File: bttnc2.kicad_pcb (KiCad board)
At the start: 2 copper layers, 72 parts, among them K1 MK12C02, P1 ISP, P2 BATTERY, P3 BNC, P4 USB_OTG, SW1 SW_PUSH, U1 HC-05, U2 APE8800N, U3 BU33TD3WG, U4 ATMEGA328P-AU, U5 DRA818V, U6 DW01-P, U7 TP4056, U8 8205A, X1 QKT-3225SMD 16.0000MHz

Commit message: Update bttnc project. Sch and Pcb files.
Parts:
- added C25: C, Capacitors_SMD:C_0805, B.Cu at (140.9, 109.5)
- added C26: C, Capacitors_SMD:C_0805, B.Cu at (135.3, 116.5)
- added C27: CP1, Capacitors_SMD:C_1206, F.Cu at (158.4, 130.7)
- added C28: C, Capacitors_SMD:C_0805, B.Cu at (158.4, 132.0)
- added C29: C, Capacitors_SMD:C_0805, F.Cu at (159.5, 136.9)
- added C30: CP1, Capacitors_SMD:C_1206, F.Cu at (159.5, 134.5)
- added C31: C, Capacitors_SMD:C_0805, B.Cu at (149.9, 128.5)
- added C32: CP1, Capacitors_SMD:C_1206, B.Cu at (152.3, 129.0)
- added D10: D_Schottky, Diodes_SMD:MiniMELF_Standard, B.Cu at (158.0, 127.3)
- added D11: D_Schottky, Diodes_SMD:MiniMELF_Standard, B.Cu at (155.3, 127.3)
- added D5: D_Schottky, Diodes_SMD:MiniMELF_Standard, B.Cu at (159.9, 107.7)
- added D6: D_Schottky, Diodes_SMD:MiniMELF_Standard, B.Cu at (124.7, 120.6)
- added D7: D_Schottky, Diodes_SMD:MiniMELF_Standard, B.Cu at (155.3, 133.0)
- added D8: LED, LEDs:LED_0805, F.Cu at (104.5, 137.9)
- added D9: D_Schottky, Diodes_SMD:MiniMELF_Standard, B.Cu at (149.7, 133.0)
- added Q1: MMBT3904, TO_SOT_Packages_SMD:SOT-23, B.Cu at (107.8, 137.8)
- added R19: R, Resistors_SMD:R_0805, B.Cu at (125.5, 122.9)
- added R20: R, Resistors_SMD:R_0805, B.Cu at (138.9, 121.7)
- added R21: R, Resistors_SMD:R_0805, F.Cu at (138.4, 116.5)
- added R22: R, Resistors_SMD:R_0805, B.Cu at (151.6, 124.6)
- added R23: R, Resistors_SMD:R_0805, B.Cu at (108.2, 134.9)
- added R24: R, Resistors_SMD:R_0805, B.Cu at (148.0, 128.4)
- added R25: R, Resistors_SMD:R_0805, B.Cu at (160.9, 129.8)
- added R26: R, Resistors_SMD:R_0805, F.Cu at (159.4, 124.6)
- added R27: R, Resistors_SMD:R_0805, B.Cu at (160.9, 126.4)
- added U10: Quectel-L80, footprints:Qectel-L80, F.Cu at (147.6, 130.9)
- added U11: FDG6342L, TO_SOT_Packages_SMD:SC-70-6, F.Cu at (159.4, 127.0)
- added U9: LM358, SMD_Packages:SOIC-8-N, B.Cu at (139.0, 116.3)
- C1, C15, C16, C17, C19, C2, C22, C23, C24, C3, C5, C6, C7, C8, C9, FB1, FB2, FB3, FB6, FB8, R12, R13, R15, R17, R18, R3, R4, R5, R8, R9, U2, U3, U4, U7, U8, X1: moved to B.Cu
- P3: footprint SMD_Packages:SOIC-8-N -> footprints:CON-SMA-EDGE
- SW1: footprint footprints:B3FS-1002P -> Buttons_Switches_ThroughHole:SW_Tactile_SPST_Angled
- moved K1 217.4 mm to (166.4, 139.9)
- moved U8 214.9 mm to (166.5, 135.9), turned to 180 degrees
- moved P2 213.2 mm to (169.4, 129.5), turned to 270 degrees
- moved C20 212.7 mm to (164.8, 134.4)
- moved C19 212.2 mm to (167.2, 130.6), turned to 270 degrees
- moved U6 210.8 mm to (164.9, 131.3), turned to 270 degrees
- moved R12 210.3 mm to (165.0, 130.4), turned to 90 degrees
- moved R14 208.8 mm to (162.3, 131.3), turned to 270 degrees
- moved P4 208.1 mm to (168.6, 122.0), turned to 90 degrees
- moved R18 207.5 mm to (163.7, 127.5)
- moved D4 207.4 mm to (163.7, 127.4), turned to 180 degrees
- moved D2 206.3 mm to (163.7, 125.5), turned to 180 degrees
- moved R17 206.3 mm to (163.7, 125.5), turned to 180 degrees
- moved C21 204.5 mm to (164.1, 122.0), turned to 90 degrees
- moved R13 203.8 mm to (164.7, 120.0), turned to 270 degrees
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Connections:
- C2 pad 1: SPK -> Net-(C2-Pad1)
- FB1 pad 1: RF_RXD -> TXD
- FB2 pad 1: RF_TXD -> Net-(D6-Pad1)
- R11 pad 1: SPK -> GND
- R11 pad 2: GND -> Net-(C26-Pad2)
- R8 pad 1: VCC -> Net-(R20-Pad2)
- U1 pad 1: Net-(U1-Pad1) -> Net-(D5-Pad1)
- U1 pad 2: Net-(U1-Pad2) -> TXD
- U4 pad 13: Net-(U4-Pad13) -> RF_SQ
- U4 pad 25: RF_TXD -> Net-(U4-Pad25)
- U4 pad 26: RF_RXD -> GPS_RESET
- U4 pad 30: Net-(U1-Pad1) -> RXD
- U4 pad 31: Net-(U1-Pad2) -> TXD
- U4 pad 9: Net-(U4-Pad9) -> GPS_EN
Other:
- board outline added: 70 x 40 mm

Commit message: Latest updates
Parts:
- C20, R14, U6: moved to B.Cu
- C21: footprint Capacitors_SMD:C_1210 -> Capacitors_SMD:C_0805
- R13, U7: moved to F.Cu
- moved R25 26.2 mm to (135.3, 124.1), turned to 0 degrees
- moved D10 18.2 mm to (140.0, 124.5), turned to 180 degrees
- moved D4 17.3 mm to (170.2, 111.4), turned to 90 degrees
- moved R13 15.4 mm to (164.2, 135.4), turned to 180 degrees
- moved D2 12.0 mm to (170.2, 115.3), turned to 270 degrees
- moved U7 9.71 mm to (164.0, 130.3), turned to 90 degrees
- moved R18 7.94 mm to (162.4, 119.7), turned to 90 degrees
- moved C20 7.52 mm to (162.8, 127.1)
- moved R17 5.89 mm to (164.4, 119.6), turned to 270 degrees
- moved R12 5.64 mm to (162.8, 125.2), turned to 0 degrees
- moved U8 5.21 mm to (166.2, 130.7), turned to 90 degrees
- moved D9 4.45 mm to (145.5, 134.5), turned to 270 degrees
- moved C19 3.93 mm to (169.4, 127.4), turned to 0 degrees
- moved D11 3.53 mm to (152.3, 129.0)
- moved R14 3.09 mm to (162.8, 134.4)
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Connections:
- C19 pad 2: Net-(C19-Pad2) -> GND
- C20 pad 2: Net-(C19-Pad2) -> Net-(C20-Pad2)
- P2 pad 2: Net-(C19-Pad2) -> Net-(C20-Pad2)
- U6 pad 6: Net-(C19-Pad2) -> Net-(C20-Pad2)
- U7 pad 9: GND -> Net-(C21-Pad1)
- U8 pad 2: Net-(C19-Pad2) -> Net-(C20-Pad2)
- U8 pad 3: Net-(C19-Pad2) -> Net-(C20-Pad2)
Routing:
- net Net-(C21-Pad1): track 0.00 -> 23.5 mm
- net Net-(C20-Pad2): track 0.00 -> 12.1 mm
- net Net-(U6-Pad3): track 0.00 -> 9.13 mm, vias 0 -> 2
- net Net-(C19-Pad1): track 0.00 -> 7.77 mm
- net Net-(U6-Pad1): track 0.00 -> 3.28 mm
- net Net-(R13-Pad2): track 0.00 -> 2.41 mm
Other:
- rule via_min_drill: 0.508 -> 0.127

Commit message: Initial pcb routing
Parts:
- added C33: C, Capacitors_SMD:C_0805, F.Cu at (132.7, 132.3)
- added C34: C, Capacitors_SMD:C_0805, F.Cu at (132.7, 134.3)
- added P5: BNC, footprints:U.FL-Coax, F.Cu at (135.7, 129.2)
- added P6: CONN_01X03, Pin_Headers:Pin_Header_Straight_1x03_Pitch2.54mm, F.Cu at (150.3, 120.0)
- added R28: R, Resistors_SMD:R_0805, F.Cu at (135.7, 133.2)
- moved D11 9.14 mm to (145.8, 122.6), turned to 90 degrees
- moved C11 4.62 mm to (134.6, 138.4), turned to 270 degrees
- moved R9 3.52 mm to (155.4, 114.1), turned to 0 degrees
- moved R23 2.08 mm to (106.1, 134.8)
- moved Q1 1.63 mm to (106.3, 137.8), turned to 180 degrees
- moved C10 1.32 mm to (131.7, 138.8), turned to 270 degrees
- moved D8 1.09 mm to (103.5, 137.6)
- moved R24 1.02 mm to (146.6, 129.3)
- moved C31 0.81 mm to (148.6, 129.3)
- moved C32 0.79 mm to (150.8, 129.3)
- moved R5 0.50 mm to (118.8, 106.3)
- moved R12 0.19 mm to (162.6, 125.2)
- moved R26 0.18 mm to (158.8, 124.2)
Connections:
- U4 pad 14: DPTT -> Net-(U4-Pad14)
- U4 pad 25: Net-(U4-Pad25) -> DPTT
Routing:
- net GND: track 0.00 -> 233.3 mm, vias 0 -> 58
- net +BATT: track 0.00 -> 153.1 mm, vias 0 -> 11
- net TXD: track 0.00 -> 118.4 mm, vias 0 -> 3
- net Net-(R10-Pad1): track 0.00 -> 92.1 mm, vias 0 -> 2
- net RXD: track 0.00 -> 85.7 mm
- net Net-(U1-Pad34): track 0.00 -> 71.9 mm, vias 0 -> 3
- net Net-(C27-Pad1): track 0.00 -> 70.6 mm, vias 0 -> 4
- net Net-(Q1-Pad1): track 0.00 -> 62.2 mm, vias 0 -> 4
- net VCC: track 0.00 -> 56.3 mm, vias 0 -> 2
- net GPS_EN: track 0.00 -> 53.0 mm, vias 0 -> 2
- net ENABLE: track 0.00 -> 50.0 mm, vias 0 -> 2
- net Net-(U1-Pad11): track 0.00 -> 46.0 mm, vias 0 -> 1
- net SCK: track 0.00 -> 41.1 mm
- net Net-(R16-Pad1): track 0.00 -> 39.9 mm, vias 0 -> 3
- net Net-(SW1-Pad2): track 0.00 -> 32.7 mm
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- added copper zone on B.Cu, net GND
- added copper zone on F.Cu, net GND

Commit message: Update pcb
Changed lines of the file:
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@@
     (links 225)
     (no_connects 0)
-    (area 101.143999 101.143999 171.294001 141.299001)
+    (area 93.497399 97.941666 174.5215 142.519501)
     (thickness 1.6)
     (drawings 4)
@@
   )
   (setup
-    (last_trace_width 0.3)
+    (last_trace_width 0.254)
     (user_trace_width 0.3)
     (user_trace_width 0.5)
@@
   (segment (start 144.1196 108.712) (end 147.5232 108.712) (width 0.3) (layer B.Cu) (net 4))
   (segment (start 143.957 108.8746) (end 144.1196 108.712) (width 0.3) (layer B.Cu) (net 4))
-  (segment (start 117.8712 106.2863) (end 116.6749 106.2863) (width 0.3) (layer B.Cu) (net 5) (status 400000))
+  (segment (start 117.8712 106.2863) (end 116.6749 106.2863) (width 0.3) (layer B.Cu) (net 5))
   (via (at 112.0902 109.8042) (size 0.9) (drill 0.35) (layers F.Cu B.Cu) (net 5))
   (segment (start 116.586 109.8042) (end 112.0902 109.8042) (width 0.3) (layer F.Cu) (net 5))
@@
   (segment (start 135.7376 134.5692) (end 135.7376 134.1476) (width 0.5) (layer F.Cu) (net 114))
   (segment (start 135.89 134.7216) (end 135.7376 134.5692) (width 0.5) (layer F.Cu) (net 114))
-  (zone (net 0) (net_name "") (layer F.Cu) (hatch edge 0.508)
-    (connect_pads (clearance 0.508))
-    (min_thickness 0.254)
-    (keepout (tracks not_allowed) (vias not_allowed) (copperpour allowed))
-    (fill (arc_segments 16) (thermal_gap 0.508) (thermal_bridge_width 0.508))
-    (polygon
-      (pts
-        (xy 171.196 116.6876) (xy 162.7632 116.6876) (xy 162.7632 101.2444) (xy 171.196 101.2444)
-      )
-    )
-  )
-  (zone (net 0) (net_name "") (layer B.Cu) (hatch edge 0.508)
-    (connect_pads (clearance 0.508))
-    (min_thickness 0.254)
-    (keepout (tracks not_allowed) (vias not_allowed) (copperpour allowed))
-    (fill (arc_segments 16) (thermal_gap 0.508) (thermal_bridge_width 0.508))
-    (polygon
-      (pts
-        (xy 171.196 116.6876) (xy 162.7632 116.6876) (xy 162.7632 101.1936) (xy 171.196 101.1936)
-      )
-    )
-  )
   (zone (net 5) (net_name GND) (layer F.Cu) (hatch edge 0.508)
     (connect_pads (clearance 0.508))
@@
     (polygon
       (pts
-        (xy 171.0944 141.1224) (xy 101.2952 141.1224) (xy 101.2952 101.2952) (xy 171.0944 101.2952)
+        (xy 163.4236 117.0686) (xy 171.1071 117.0686) (xy 171.1071 141.1351) (xy 101.3079 141.1351) (xy 101.3079 101.3079)
+        (xy 163.4236 101.3079)
       )
     )
@@
     (polygon
       (pts
-        (xy 171.0944 141.1224) (xy 101.2952 141.1224) (xy 101.2952 101.2952) (xy 171.0944 101.2952)
+        (xy 163.4236 117.0686) (xy 171.1071 117.0686) (xy 171.1071 141.1351) (xy 101.3079 141.1351) (xy 101.3079 101.3079)
+        (xy 163.4236 101.3079)
       )
     )

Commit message: Updated SMA connector
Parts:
- moved P3 0.13 mm to (103.4, 126.5)
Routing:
- net (no net): track 8.91 -> 0.00 mm, vias 2 -> 0
- net GND: track 233.3 -> 240.0 mm, vias 58 -> 59

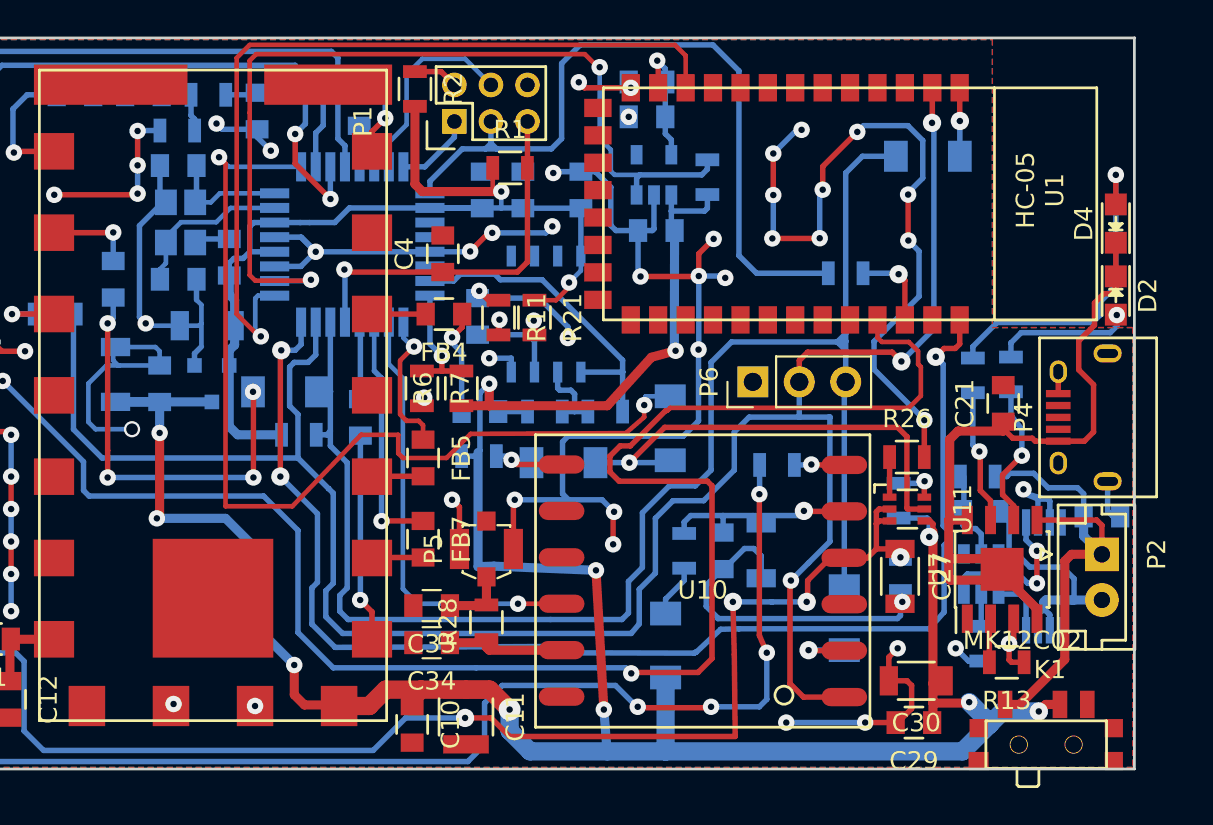
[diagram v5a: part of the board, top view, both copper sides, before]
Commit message: Improve ground planes
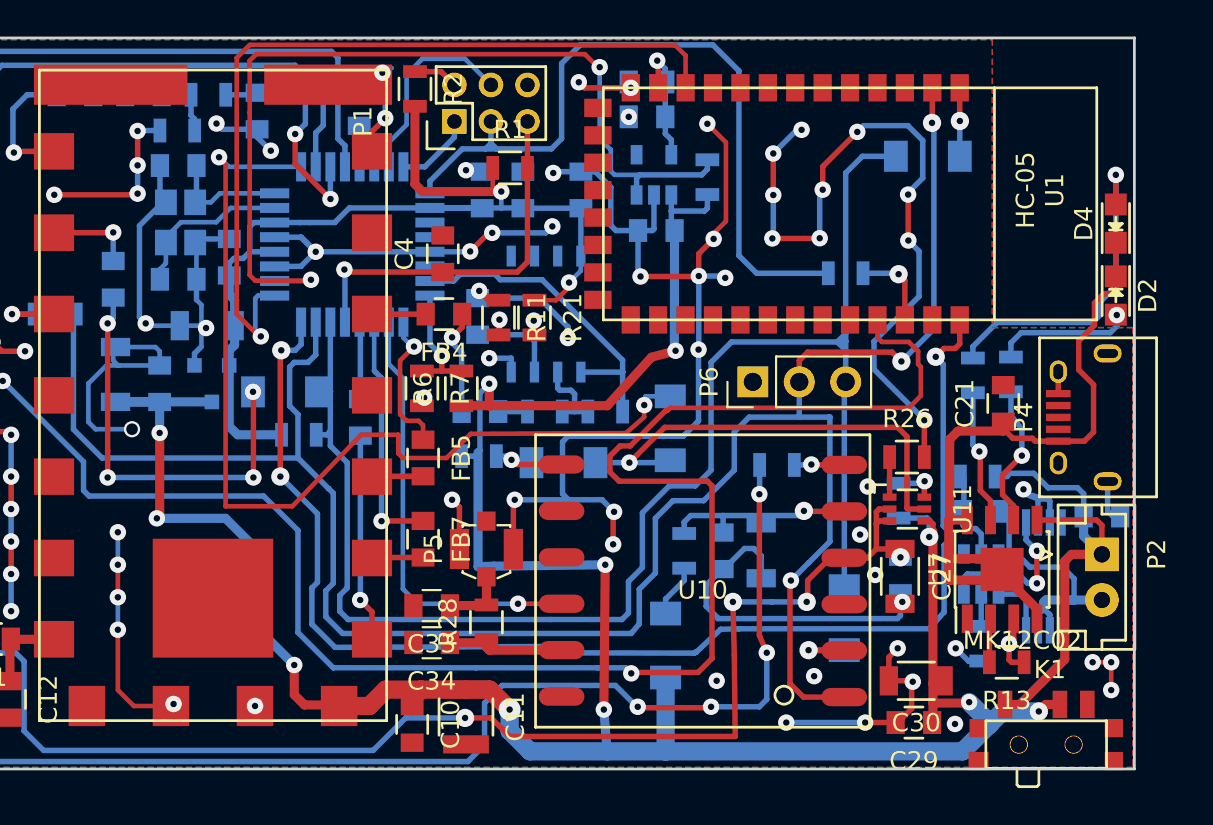
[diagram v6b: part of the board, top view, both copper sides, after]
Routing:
- net GND: track 240.0 -> 268.7 mm, vias 59 -> 71
- net +BATT: track 153.1 -> 153.9 mm
- net (no net): track 0.00 -> 0.32 mm, vias 0 -> 6

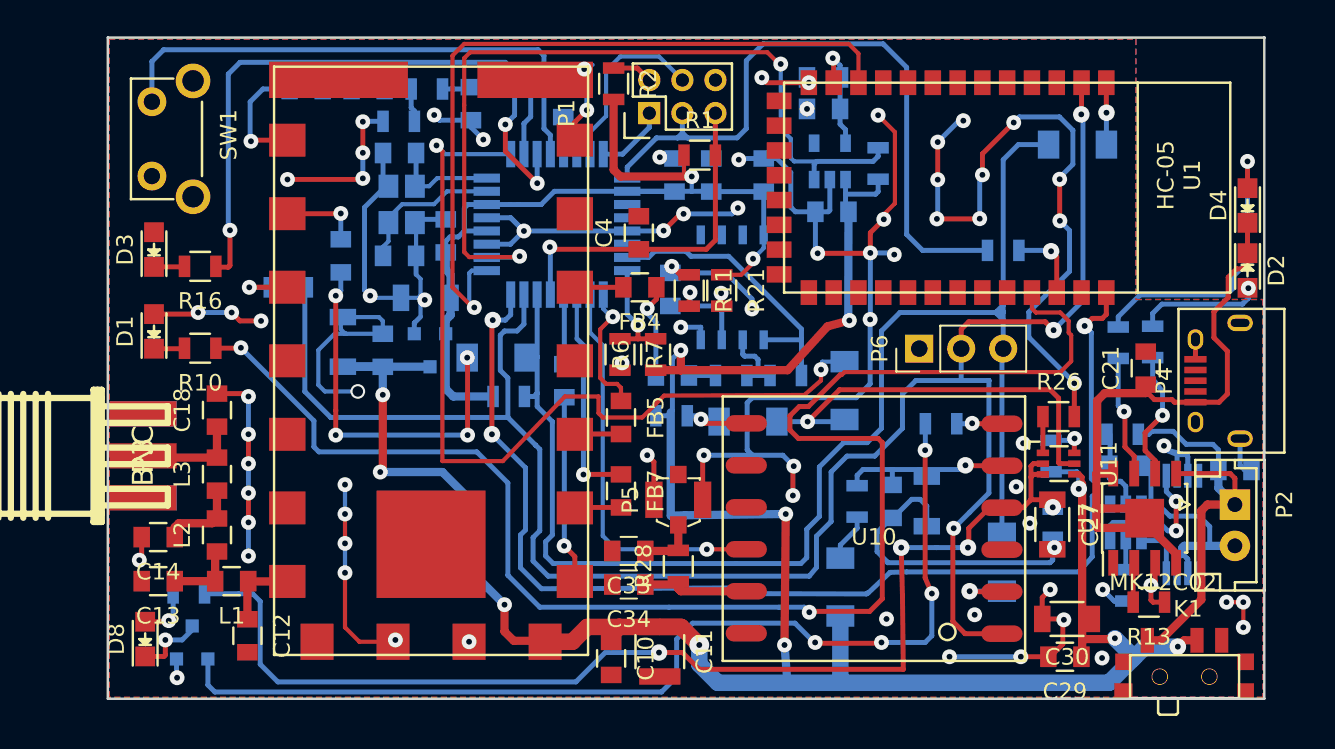
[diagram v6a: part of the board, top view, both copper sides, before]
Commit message: PCB reference labels rearrange
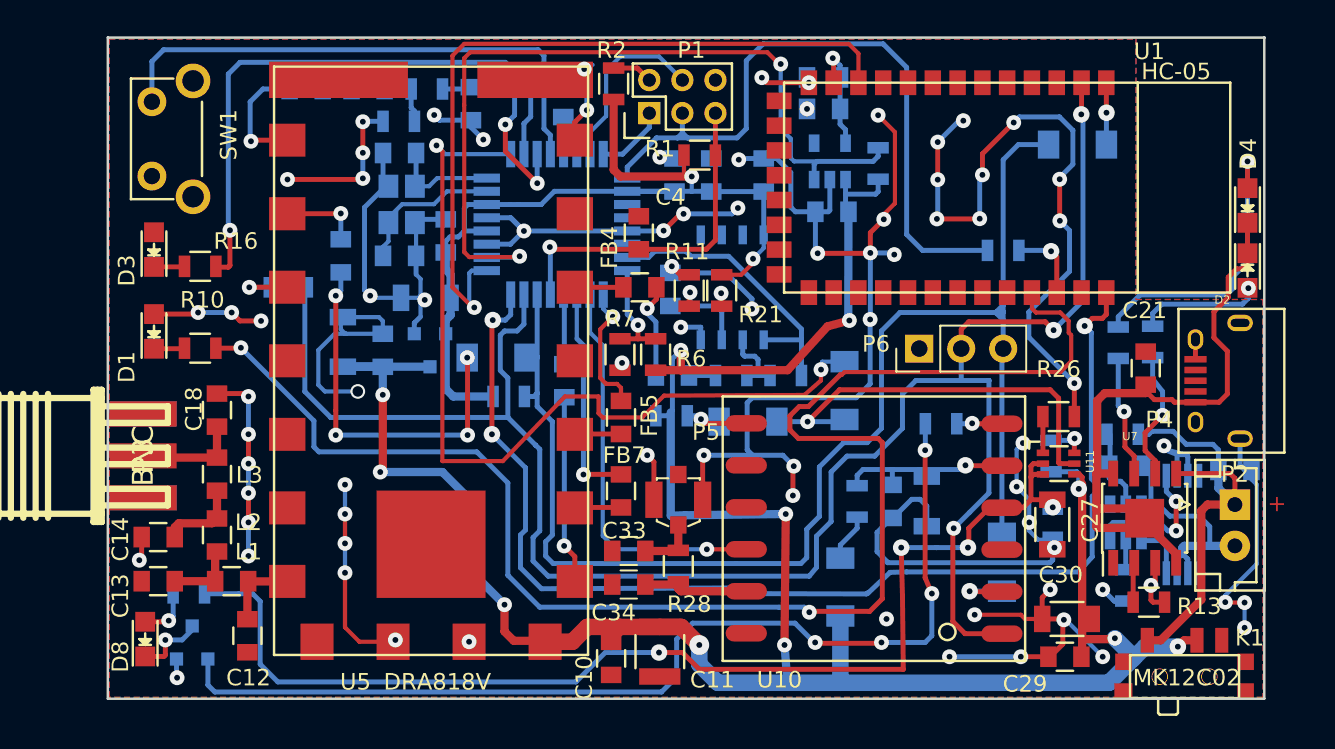
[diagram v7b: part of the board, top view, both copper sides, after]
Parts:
- D1: value Blue LED -> LED
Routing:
- net GND: track 268.7 -> 292.7 mm, vias 71 -> 76
- net (no net): track 0.32 -> 0.00 mm, vias 6 -> 1
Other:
- board text added: "+"
